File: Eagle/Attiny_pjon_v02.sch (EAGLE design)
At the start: 16 parts, among them IC2 78L05SMD

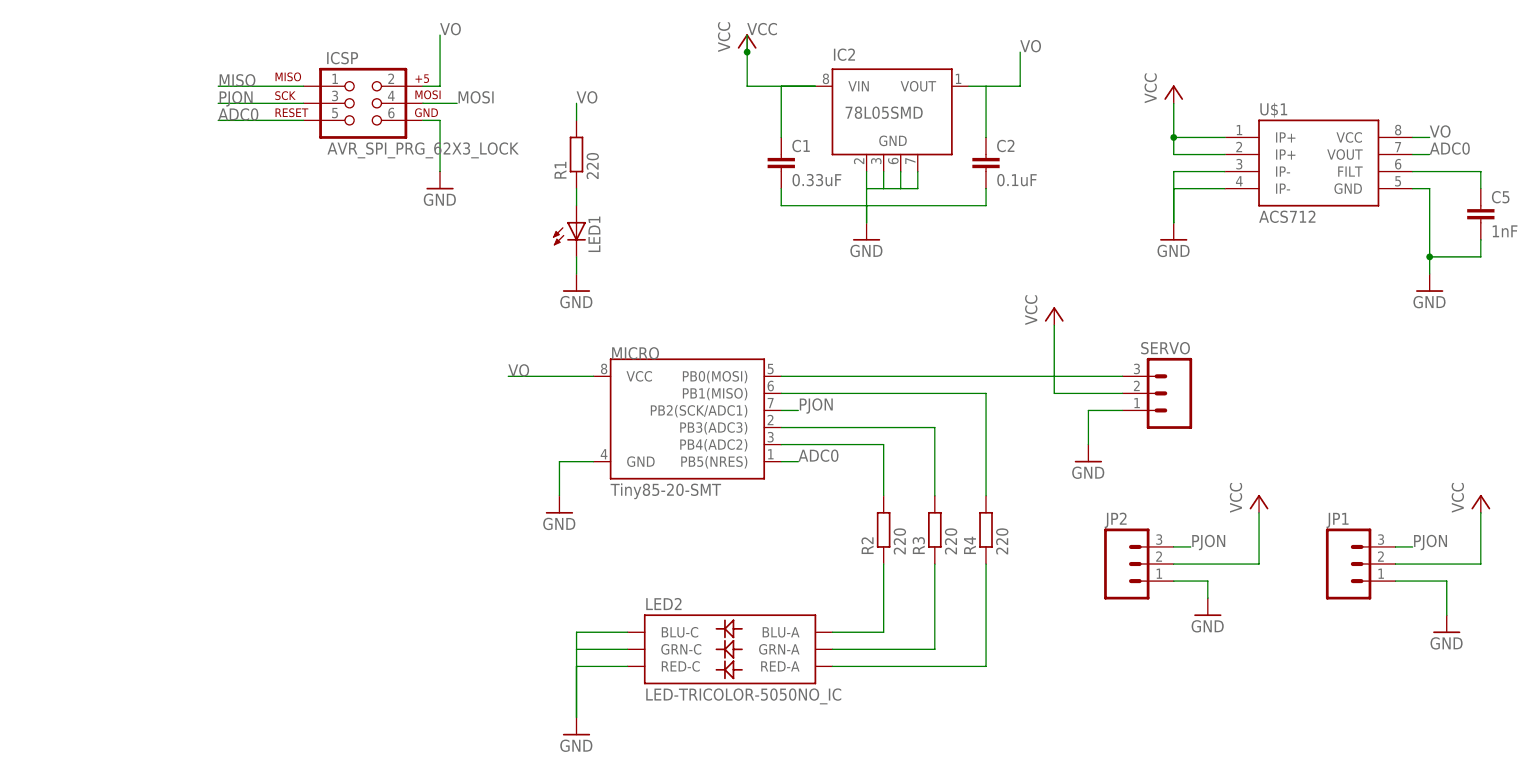
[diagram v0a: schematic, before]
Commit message: Board V0.2
RGB LED Removed.
Added external oscillator, temperature sensor and a center hole
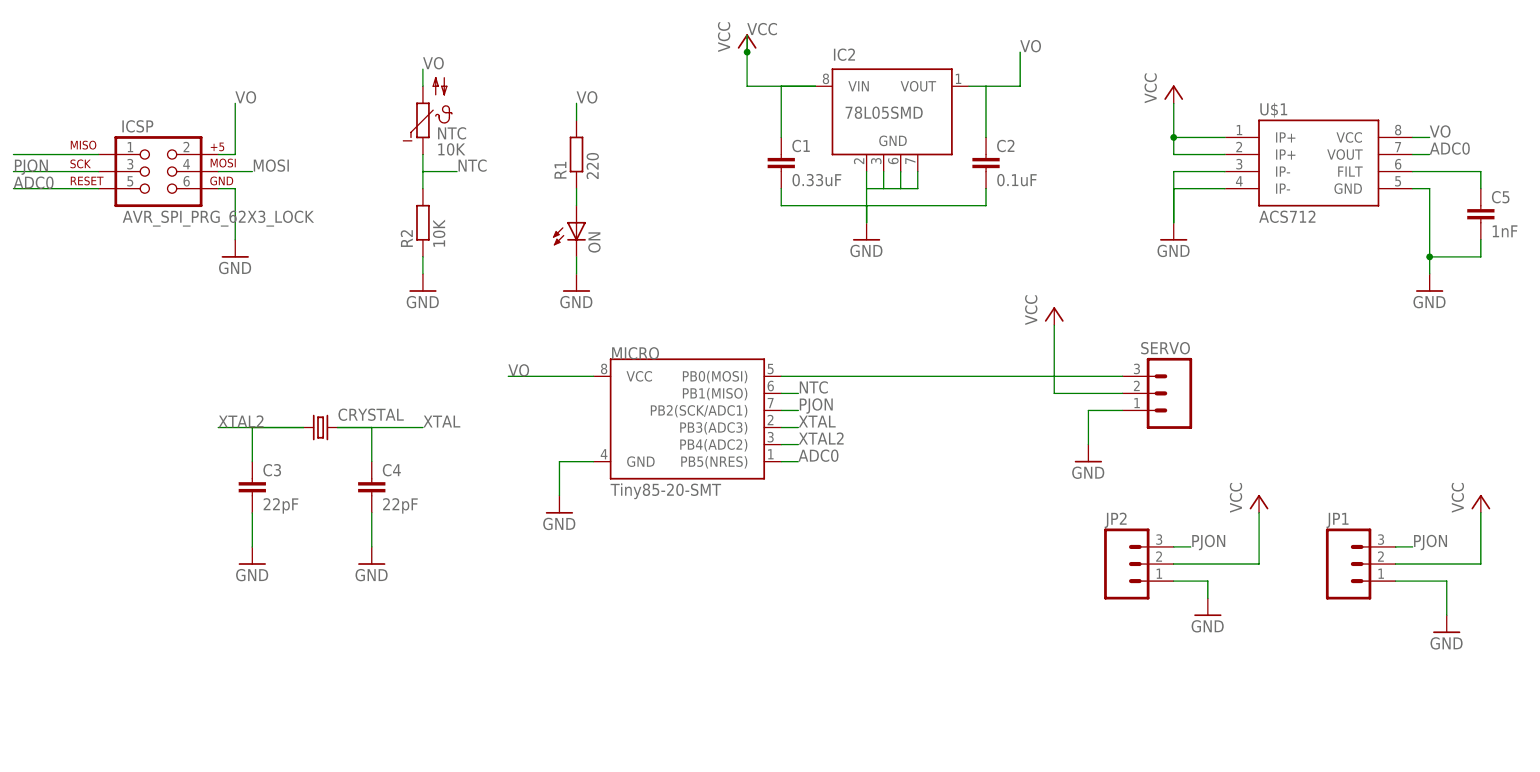
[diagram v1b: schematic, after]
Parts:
- removed LED2: LED-TRICOLOR-5050NO_IC, SparkFun-LED:LED-TRICOLOR-5050NO_IC
- removed R3, R4: 220, resistor:R-EU_R1206
- added C3, C4: 22pF, rcl:C-EUC1206
- added CRYSTAL: (no value), SparkFun-FreqCtrl:CRYSTALSMD
- added NTC: 10K, ptc-ntc:NTC640
- R2: value 220 -> 10K
- renumbered LED1 to ON
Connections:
- removed net N$1: MICRO.PB4(ADC2), R2.2
- removed net N$3: MICRO.PB3(ADC3), R3.2
- removed net N$4: LED2.BLU-A, R2.1
- removed net N$5: LED2.GRN-A, R3.1
- removed net N$7: LED2.RED-A, R4.1
- new net NTC: MICRO.PB1(MISO), NTC.1, R2.2
- new net XTAL: C4.1, CRYSTAL.2, MICRO.PB3(ADC3)
- new net XTAL2: C3.1, CRYSTAL.1, MICRO.PB4(ADC2)
- net GND: now also C3.2, C4.2, R2.1; no longer LED2.BLU-C, LED2.GRN-C, LED2.RED-C
- net MISO: no longer MICRO.PB1(MISO), R4.2
- net VO: now also NTC.2
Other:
- moved on the sheet: ICSP, R2

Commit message: Scheme V02
Fixed an issue related with voltage regulator, tested in bread board
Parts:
- removed NTC: 10K, ptc-ntc:NTC640
- removed R2: 10K, resistor:R-EU_R1206
- added D1: SS12, SparkFun-DiscreteSemi:DIODE-SCHOTTKY-B340A
- renumbered JP2 to PJON, U$1 to IC3
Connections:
- removed net NTC: MICRO.PB1(MISO), NTC.1, R2.2
- new net ADC1: IC3.VOUT, MICRO.PB2(SCK/ADC1)
- new net N$3: C2.1, D1.A, IC2G$1.VOUT
- net ADC0: no longer IC3.VOUT, MICRO.PB5(NRES)
- net GND: no longer R2.1
- net PJON: now also MICRO.PB1(MISO); no longer MICRO.PB2(SCK/ADC1)
- net VO: now also D1.C; no longer C2.1, IC2G$1.VOUT, NTC.2
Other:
- moved on the sheet: C1, C2, IC2, ICSP
